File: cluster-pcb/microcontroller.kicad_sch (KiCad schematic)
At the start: 4 parts

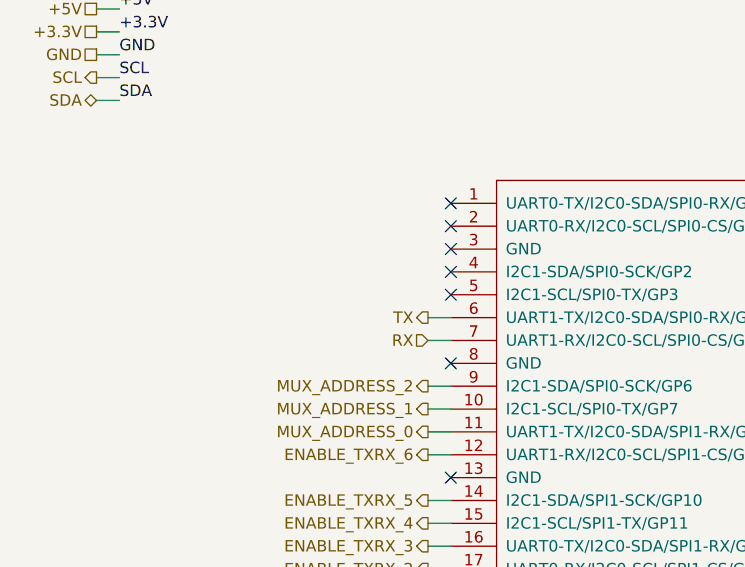
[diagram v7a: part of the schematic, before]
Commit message: Fix ERC issues
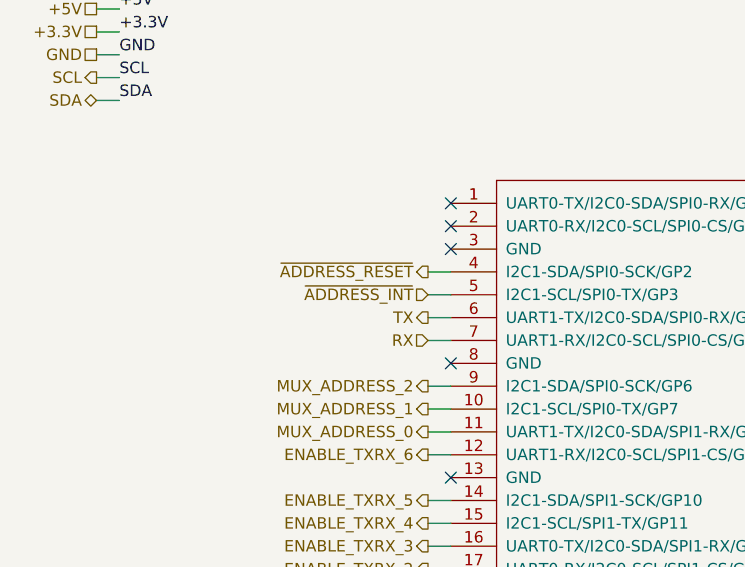
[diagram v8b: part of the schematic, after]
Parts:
- D401: footprint Janelia:DIOM3616X98N -> Janelia:SOD-123FL
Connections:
- net ~{ADDRESS_RESET}: now reaches A401.4 (I2C1-SDA/SPI0-SCK/GP2)
- net ~{ADDRESS_INT}: now reaches A401.5 (I2C1-SCL/SPI0-TX/GP3)
- no-connect marks 15 -> 13
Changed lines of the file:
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@@
   (title_block
     (title "cluster-pcb")
-    (date "2024-09-12")
+    (date "2024-09-13")
     (rev "1.2")
     (company "Howard Hughes Medical Institute")
@@
   (no_connect (at 180.34 81.28))
   (no_connect (at 93.98 71.12))
-  (no_connect (at 93.98 78.74))
   (no_connect (at 180.34 99.06))
   (no_connect (at 93.98 86.36))
   (no_connect (at 180.34 68.58))
-  (no_connect (at 93.98 76.2))
   (no_connect (at 180.34 86.36))
   (no_connect (at 180.34 93.98))
@@
     (stroke (width 0) (type default))
   )
+  (wire (pts (xy 91.44 76.2) (xy 93.98 76.2))
+    (stroke (width 0) (type default))
+  )
   (wire (pts (xy 91.44 109.22) (xy 93.98 109.22))
     (stroke (width 0) (type default))
@@
   )
   (wire (pts (xy 234.95 76.2) (xy 234.95 73.66))
+    (stroke (width 0) (type default))
+  )
+  (wire (pts (xy 91.44 78.74) (xy 93.98 78.74))
     (stroke (width 0) (type default))
   )
@@
     (effects (font (size 1.27 1.27)) (justify left))
   )
+  (hierarchical_label "~{ADDRESS_INT}" (shape input) (at 91.44 78.74 180) (fields_autoplaced)
+    (effects (font (size 1.27 1.27)) (justify right))
+  )
   (hierarchical_label "ENABLE_TXRX_2" (shape output) (at 91.44 109.22 180) (fields_autoplaced)
     (effects (font (size 1.27 1.27)) (justify right))
@@
   )
   (hierarchical_label "GND" (shape passive) (at 54.61 52.07 180) (fields_autoplaced)
+    (effects (font (size 1.27 1.27)) (justify right))
+  )
+  (hierarchical_label "~{ADDRESS_RESET}" (shape output) (at 91.44 76.2 180) (fields_autoplaced)
     (effects (font (size 1.27 1.27)) (justify right))
   )
@@
       (effects (font (size 1.27 1.27)) (justify left) hide)
     )
-    (property "Footprint" "Janelia:DIOM3616X98N" (at 142.24 57.912 0)
-      (effects (font (size 1.524 1.524)) hide)
-    )
+    (property "Footprint" "Janelia:SOD-123FL" (at 142.24 57.912 0)
+      (effects (font (size 1.524 1.524)) hide)
+    )
